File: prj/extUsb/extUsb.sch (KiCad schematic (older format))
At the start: 6 parts, among them J1 USB_B_Micro, J2 Conn_01x05, U1 SN74LVC2T45

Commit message: extUsb Redo after attempt2 experiments and add 3.3V rail.
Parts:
- added C1, C2: 18p, Capacitor_SMD:C_0603_1608Metric_Pad1.08x0.95mm_HandSolder, symbol Device:C
- added C3, C4: 100n, Capacitor_SMD:C_0603_1608Metric_Pad1.08x0.95mm_HandSolder, symbol Device:C
- added C5: 10u, Capacitor_SMD:C_0603_1608Metric_Pad1.08x0.95mm_HandSolder, symbol Device:C
- added FB1: Ferrite_Bead, Inductor_SMD:L_0603_1608Metric_Pad1.05x0.95mm_HandSolder, symbol Device:Ferrite_Bead
- added Q1: Q_NMOS_GSD, Package_TO_SOT_SMD:SOT-23_Handsoldering, symbol Device:Q_NMOS_GSD
- added R4: 10k, Resistor_SMD:R_0603_1608Metric_Pad0.98x0.95mm_HandSolder, symbol Device:R
- added U2: MIC5504-3.3YM5, Package_TO_SOT_SMD:SOT-23-5, symbol Regulator_Linear:MIC5504-3.3YM5
- R1: renamed from R2; value 68 -> 33
- R2: renamed from R3; value 68 -> 33
- renumbered R1 to R3
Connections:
- net labels added: +3.3V, +5V
- net labels removed: Vusb
- wire segments 29 -> 35
- no-connect marks 2 -> 1
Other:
- moved on the sheet: J1, J2, R1, R2, R3, U1

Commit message: extUsb Annotate schematic
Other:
- note added: "1.0.0"
- note added: "2020-10-31"
- note added: "FB1 blocks noise from propagating to USB host power supply,\nand works in conjunction with C5 to stabilize +5V.\nC3, C4, and C5 bypass capacitors stabilize power supplies.\nU2 provides 3.3V, as required by USB."
- note added: "J2 separated via labels to simplify pin re-assignment."
- note added: "Levelshifter for low or unknown voltage (1.65V..5.5V) logic implementing USB Full Speed protocol.\nFor example, FPGA with protocol implemented in logic, or a MCU bit-banging the protocol."
- note added: "R1 and R2 series termination protect D+,D- transmission lines against device-to-host transient voltage spikes.\nOptionally (with C1,C2) include low-pass filtering."
- note added: "R3 pullup to 3.3V indicates USB-FullSpeed to host, enabled by connecting Vext.\nWhen Vext is unconnected, R4 pulldown on Q1 disables the R3 pullup, indicating "no device" to host."
- note added: "extUsb"
- moved on the sheet: C1, C2, C3, C4, C5, FB1, J1, J2, R1, R2, R3, R4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

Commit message: extUsb Layout for hand-solder
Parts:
- U2: footprint Package_TO_SOT_SMD:SOT-23-5 -> Package_TO_SOT_SMD:SOT-23-5_HandSoldering
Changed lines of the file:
@@
 F 0 "U2" H 2900 2267 50  0000 C CNN
 F 1 "MIC5504-3.3YM5" H 2900 2176 50  0000 C CNN
-F 2 "Package_TO_SOT_SMD:SOT-23-5" H 2900 1500 50  0001 C CNN
+F 2 "Package_TO_SOT_SMD:SOT-23-5_HandSoldering" H 2900 1500 50  0001 C CNN
 F 3 "http://ww1.microchip.com/downloads/en/DeviceDoc/MIC550X.pdf" H 2650 2150 50  0001 C CNN
 	1    2900 1900

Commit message: extUsb Analog switch for 1k5 pullup
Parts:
- removed Q1: Q_NMOS_GSD, Package_TO_SOT_SMD:SOT-23_Handsoldering, symbol Device:Q_NMOS_GSD
- added U3: TS5A3166DBVR, Package_TO_SOT_SMD:SOT-23-5, symbol Analog_Switch:TS5A3166DBVR
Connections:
- wire segments 35 -> 41
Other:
- note added: "R3 pullup to 3.3V indicates USB-FullSpeed to host, enabled by connecting Vext.\nWhen Vext is unconnected, R4 pulldown on U3 disables the R3 pullup, indicating "no device" to host."
- note removed: "R3 pullup to 3.3V indicates USB-FullSpeed to host, enabled by connecting Vext.\nWhen Vext is unconnected, R4 pulldown on Q1 disables the R3 pullup, indicating "no device" to host."
- moved on the sheet: R4
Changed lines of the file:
@@
 L power:+3.3V #PWR01
 U 1 1 5FA00B0B
-P 1700 5100
-F 0 "#PWR01" H 1700 4950 50  0001 C CNN
-F 1 "+3.3V" H 1715 5273 50  0000 C CNN
-F 2 "" H 1700 5100 50  0001 C CNN
-F 3 "" H 1700 5100 50  0001 C CNN
-	1    1700 5100
+P 1050 5000
+F 0 "#PWR01" H 1050 4850 50  0001 C CNN
+F 1 "+3.3V" H 1065 5173 50  0000 C CNN
+F 2 "" H 1050 5000 50  0001 C CNN
+F 3 "" H 1050 5000 50  0001 C CNN
+	1    1050 5000
 	1    0    0    -1
 $EndComp
@@
 	1950 1800 2200 1800
 $Comp
-L Device:Q_NMOS_GSD Q1
-U 1 1 5FA2F162
-P 1600 5300
-F 0 "Q1" H 1804 5346 50  0000 L CNN
-F 1 "Q_NMOS_GSD" H 1804 5255 50  0000 L CNN
-F 2 "Package_TO_SOT_SMD:SOT-23_Handsoldering" H 1800 5400 50  0001 C CNN
-F 3 "https://www.vishay.com/docs/63302/si2342ds.pdf" H 1600 5300 50  0001 C CNN
-	1    1600 5300
-	1    0    0    -1
-$EndComp
-$Comp
 L Device:R R4
 U 1 1 5FA4650C
-P 1350 5450
-F 0 "R4" H 1400 5400 50  0000 L CNN
-F 1 "10k" V 1350 5350 50  0000 L CNN
-F 2 "Resistor_SMD:R_0603_1608Metric_Pad0.98x0.95mm_HandSolder" V 1280 5450 50  0001 C CNN
-F 3 "~" H 1350 5450 50  0001 C CNN
-	1    1350 5450
+P 1000 5550
+F 0 "R4" H 1050 5500 50  0000 L CNN
+F 1 "10k" V 1000 5450 50  0000 L CNN
+F 2 "Resistor_SMD:R_0603_1608Metric_Pad0.98x0.95mm_HandSolder" V 930 5550 50  0001 C CNN
+F 3 "~" H 1000 5550 50  0001 C CNN
+	1    1000 5550
 	1    0    0    -1
 $EndComp
 Wire Wire Line
 	1300 6100 1700 6100
-Text GLabel 1300 5300 0    50   Input ~ 0
+Text GLabel 950  5400 0    50   Input ~ 0
 Vext
 $Comp
 L power:GND #PWR0103
 U 1 1 5FA4C220
-P 1350 5600
-F 0 "#PWR0103" H 1350 5350 50  0001 C CNN
-F 1 "GND" H 1355 5427 50  0000 C CNN
-F 2 "" H 1350 5600 50  0001 C CNN
-F 3 "" H 1350 5600 50  0001 C CNN
-	1    1350 5600
+P 1000 5700
+F 0 "#PWR0103" H 1000 5450 50  0001 C CNN
+F 1 "GND" H 1005 5527 50  0000 C CNN
+F 2 "" H 1000 5700 50  0001 C CNN
+F 3 "" H 1000 5700 50  0001 C CNN
+	1    1000 5700
 	1    0    0    -1
 $EndComp
@@
 	1700 5800 1700 6100
 Wire Wire Line
-	1300 5300 1350 5300
-Connection ~ 1350 5300
+	950  5400 1000 5400
+Connection ~ 1000 5400
 Wire Wire Line
-	1350 5300 1400 5300
+	1000 5400 1050 5400
 Text Notes 1000 4800 0    50   ~ 0
-R3 pullup to 3.3V indicates USB-FullSpeed to host, enabled by connecting Vext.\nWhen Vext is unconnected, R4 pulldown on Q1 disables the R3 pullup, indicating "no device" to host.
+R3 pullup to 3.3V indicates USB-FullSpeed to host, enabled by connecting Vext.\nWhen Vext is unconnected, R4 pulldown on U3 disables the R3 pullup, indicating "no device" to host.
 Text Notes 1000 7450 0    50   ~ 0
 R1 and R2 series termination protect D+,D- transmission lines against device-to-host transient voltage spikes.\nOptionally (with C1,C2) include low-pass filtering.
@@
 Text Notes 10600 7650 0    50   ~ 0
 1.0.0
+$Comp
+L Analog_Switch:TS5A3166DBVR U3
+U 1 1 5FA73056
+P 1350 5300
+F 0 "U3" H 1250 5450 50  0000 L CNN
+F 1 "TS5A3166DBVR" H 1150 5200 50  0000 L CNN
+F 2 "Package_TO_SOT_SMD:SOT-23-5" H 1300 5150 50  0001 C CNN
+F 3 " http://www.ti.com/lit/ds/symlink/ts5a3166.pdf" H 1350 5400 50  0001 C CNN
+	1    1350 5300
+	1    0    0    -1
+$EndComp
+Wire Wire Line
+	1450 5600 1450 5700
+Wire Wire Line
+	1450 5700 1000 5700
+Connection ~ 1000 5700
+Wire Wire Line
+	1050 5300 1050 5000
+Wire Wire Line
+	1050 5000 1450 5000
+Connection ~ 1050 5000
+Wire Wire Line
+	1650 5300 1700 5300
+Wire Wire Line
+	1700 5300 1700 5500
 $EndSCHEMATC

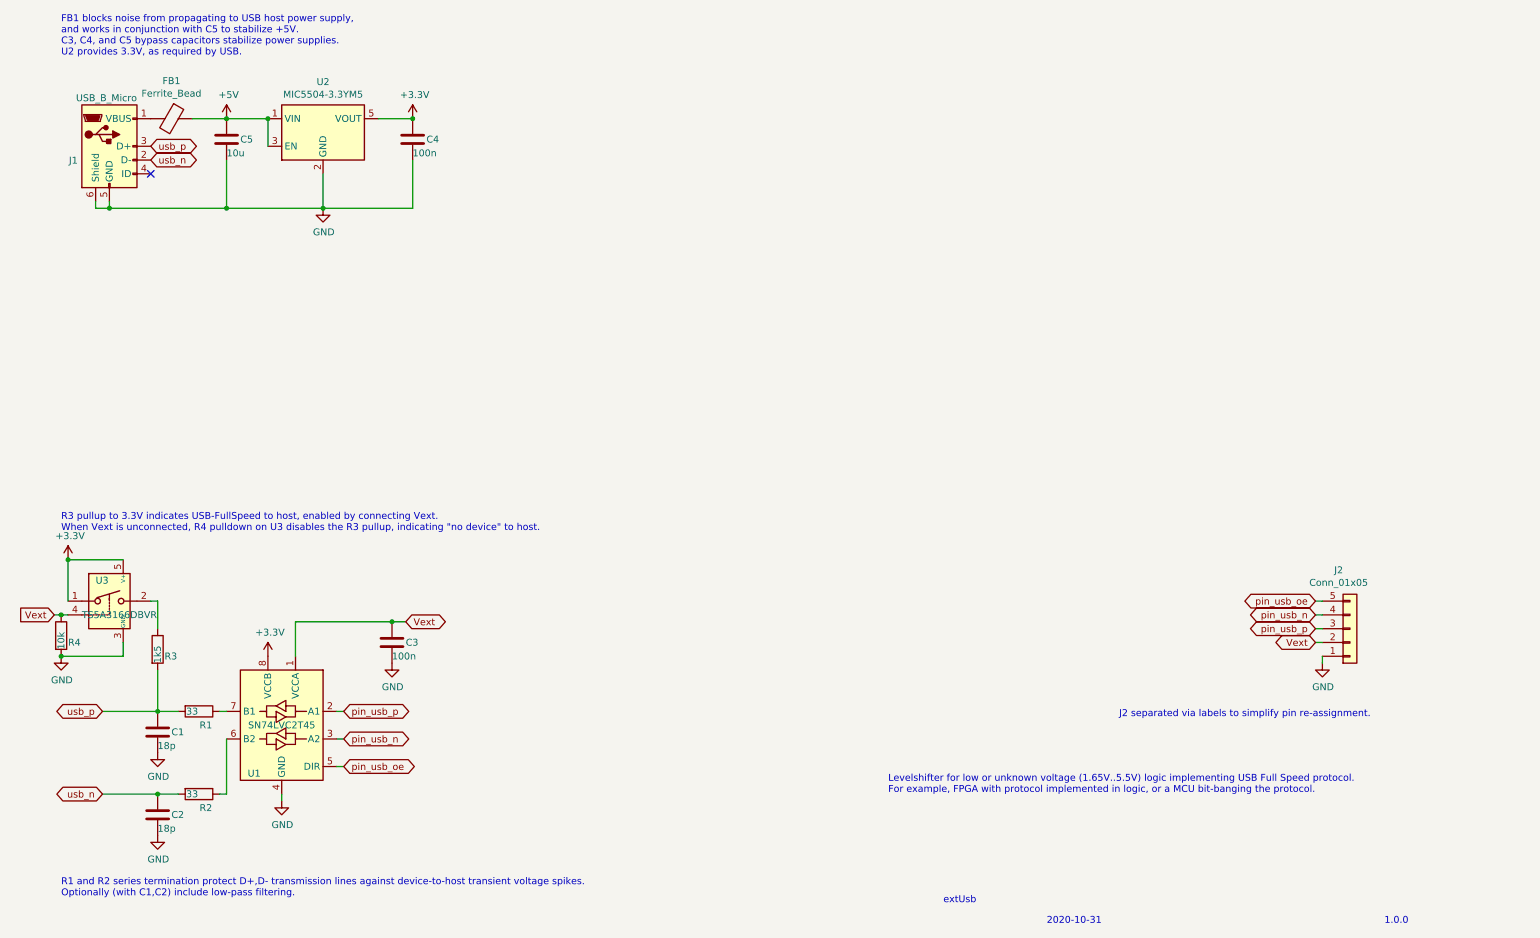
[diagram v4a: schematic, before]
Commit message: extUsb Testpoints and many minor improvements to layout.
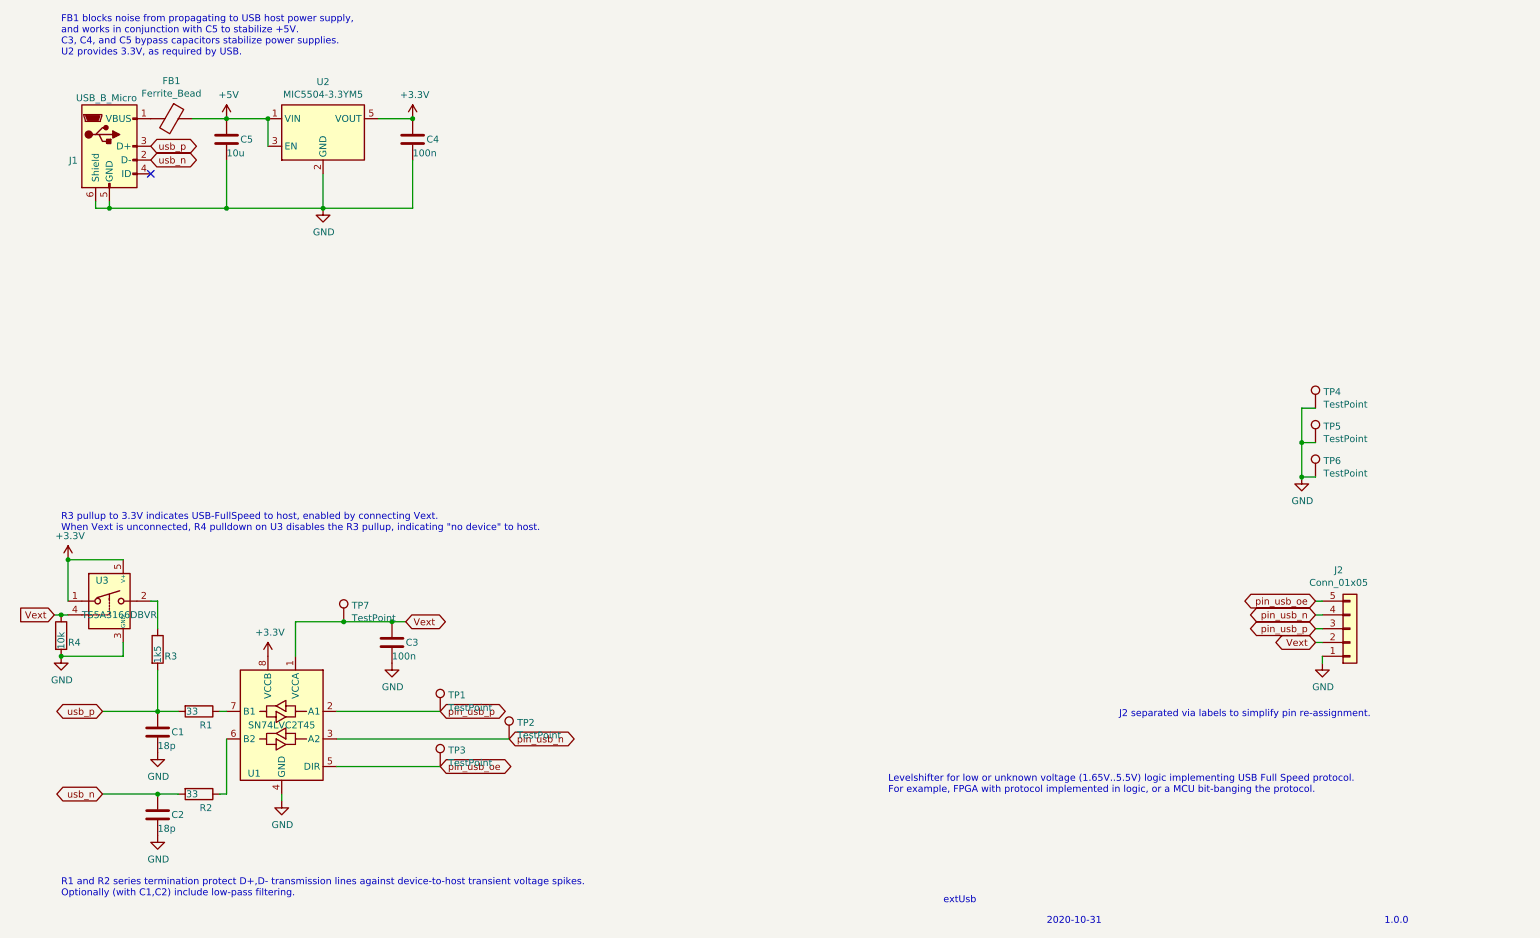
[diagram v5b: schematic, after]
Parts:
- added TP1: TestPoint, symbol Connector:TestPoint
- added TP2, TP3, TP4, TP5, TP6, TP7: TestPoint, TestPoint:TestPoint_Pad_D2.0mm, symbol Connector:TestPoint
- U3: footprint Package_TO_SOT_SMD:SOT-23-5 -> Package_TO_SOT_SMD:SOT-23-5_HandSoldering
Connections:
- net GND: now also TP4.1, TP5.1, TP6.1
- net Vext: now also TP7.1
- net pin_usb_n: now also TP2.1
- net pin_usb_oe: now also TP3.1
- net pin_usb_p: now also TP1.1
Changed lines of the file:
@@
 Text GLabel 3500 5450 2    50   BiDi ~ 0
 Vext
-Text GLabel 3050 6100 2    50   BiDi ~ 0
+Text GLabel 3750 6100 2    50   BiDi ~ 0
 pin_usb_p
-Text GLabel 3050 6300 2    50   BiDi ~ 0
+Text GLabel 4250 6300 2    50   BiDi ~ 0
 pin_usb_n
-Text GLabel 3050 6500 2    50   BiDi ~ 0
+Text GLabel 3750 6500 2    50   BiDi ~ 0
 pin_usb_oe
 Text GLabel 10100 5500 0    50   BiDi ~ 0
@@
 Text GLabel 10100 5300 0    50   BiDi ~ 0
 pin_usb_oe
-Wire Wire Line
-	3000 6100 3050 6100
-Wire Wire Line
-	3000 6300 3050 6300
-Wire Wire Line
-	3000 6500 3050 6500
 Wire Wire Line
 	10150 5300 10100 5300
@@
 	1    0    0    -1
 $EndComp
-Wire Wire Line
-	3300 1800 3550 1800
 Connection ~ 3550 1800
 $Comp
@@
 	1    0    0    -1
 $EndComp
-Wire Wire Line
-	2200 1800 2500 1800
 Connection ~ 2500 1800
 Wire Wire Line
@@
 $EndComp
 Wire Wire Line
-	3400 5450 2700 5450
-Wire Wire Line
 	2700 5450 2700 5700
 $Comp
@@
 Wire Wire Line
 	1700 6700 1850 6700
-Wire Wire Line
-	1300 6700 1700 6700
 $Comp
 L Logic_LevelTranslator:SN74LVC2T45DCUR U1
@@
 	1    0    0    -1
 $EndComp
-Wire Wire Line
-	1300 6100 1700 6100
 Text GLabel 950  5400 0    50   Input ~ 0
 Vext
@@
 Text Notes 10600 7650 0    50   ~ 0
 1.0.0
+Wire Wire Line
+	1450 5600 1450 5700
+Wire Wire Line
+	1450 5700 1000 5700
+Connection ~ 1000 5700
+Wire Wire Line
+	1050 5300 1050 5000
+Wire Wire Line
+	1050 5000 1450 5000
+Connection ~ 1050 5000
+Wire Wire Line
+	1650 5300 1700 5300
+Wire Wire Line
+	1700 5300 1700 5500
 $Comp
 L Analog_Switch:TS5A3166DBVR U3
@@
 F 0 "U3" H 1250 5450 50  0000 L CNN
 F 1 "TS5A3166DBVR" H 1150 5200 50  0000 L CNN
-F 2 "Package_TO_SOT_SMD:SOT-23-5" H 1300 5150 50  0001 C CNN
+F 2 "Package_TO_SOT_SMD:SOT-23-5_HandSoldering" H 1300 5150 50  0001 C CNN
 F 3 " http://www.ti.com/lit/ds/symlink/ts5a3166.pdf" H 1350 5400 50  0001 C CNN
 	1    1350 5300
@@
 $EndComp
 Wire Wire Line
-	1450 5600 1450 5700
-Wire Wire Line
-	1450 5700 1000 5700
-Connection ~ 1000 5700
-Wire Wire Line
-	1050 5300 1050 5000
-Wire Wire Line
-	1050 5000 1450 5000
-Connection ~ 1050 5000
-Wire Wire Line
-	1650 5300 1700 5300
-Wire Wire Line
-	1700 5300 1700 5500
+	3400 5450 3050 5450
+Wire Wire Line
+	3300 1800 3550 1800
+Wire Wire Line
+	2200 1800 2500 1800
+$Comp
+L Connector:TestPoint TP2
+U 1 1 5FA881AA
+P 4250 6300
+F 0 "TP2" H 4308 6418 50  0000 L CNN
+F 1 "TestPoint" H 4308 6327 50  0000 L CNN
+F 2 "TestPoint:TestPoint_Pad_D2.0mm" H 4450 6300 50  0001 C CNN
+F 3 "~" H 4450 6300 50  0001 C CNN
+	1    4250 6300
+	1    0    0    -1
+$EndComp
+$Comp
+L Connector:TestPoint TP1
+U 1 1 5FA87D46
+P 3750 6100
+F 0 "TP1" H 3808 6218 50  0000 L CNN
+F 1 "TestPoint" H 3808 6127 50  0000 L CNN
+F 2 "" H 3950 6100 50  0001 C CNN
+F 3 "~" H 3950 6100 50  0001 C CNN
+	1    3750 6100
+	1    0    0    -1
+$EndComp
+Wire Wire Line
+	3000 6100 3750 6100
+Wire Wire Line
+	1300 6700 1700 6700
+Wire Wire Line
+	1300 6100 1700 6100
+Wire Wire Line
+	3000 6300 4250 6300
+$Comp
+L Connector:TestPoint TP4
+U 1 1 5FAA3783
+P 10100 3900
+F 0 "TP4" H 10158 4018 50  0000 L CNN
+F 1 "TestPoint" H 10158 3927 50  0000 L CNN
+F 2 "TestPoint:TestPoint_Pad_D2.0mm" H 10300 3900 50  0001 C CNN
+F 3 "~" H 10300 3900 50  0001 C CNN
+	1    10100 3900
+	1    0    0    -1
+$EndComp
+$Comp
+L Connector:TestPoint TP5
+U 1 1 5FAA3DCC
+P 10100 4150
+F 0 "TP5" H 10158 4268 50  0000 L CNN
+F 1 "TestPoint" H 10158 4177 50  0000 L CNN
+F 2 "TestPoint:TestPoint_Pad_D2.0mm" H 10300 4150 50  0001 C CNN
+F 3 "~" H 10300 4150 50  0001 C CNN
+	1    10100 4150
+	1    0    0    -1
+$EndComp
+$Comp
+L Connector:TestPoint TP6
+U 1 1 5FAA4E02
+P 10100 4400
+F 0 "TP6" H 10158 4518 50  0000 L CNN
+F 1 "TestPoint" H 10158 4427 50  0000 L CNN
+F 2 "TestPoint:TestPoint_Pad_D2.0mm" H 10300 4400 50  0001 C CNN
+F 3 "~" H 10300 4400 50  0001 C CNN
+	1    10100 4400
+	1    0    0    -1
+$EndComp
+$Comp
+L Connector:TestPoint TP3
+U 1 1 5FAA52CF
+P 3750 6500
+F 0 "TP3" H 3808 6618 50  0000 L CNN
+F 1 "TestPoint" H 3808 6527 50  0000 L CNN
+F 2 "TestPoint:TestPoint_Pad_D2.0mm" H 3950 6500 50  0001 C CNN
+F 3 "~" H 3950 6500 50  0001 C CNN
+	1    3750 6500
+	1    0    0    -1
+$EndComp
+Wire Wire Line
+	3000 6500 3750 6500
+$Comp
+L power:GND #PWR0104
+U 1 1 5FAA8E6F
+P 10000 4400
+F 0 "#PWR0104" H 10000 4150 50  0001 C CNN
+F 1 "GND" H 10005 4227 50  0000 C CNN
+F 2 "" H 10000 4400 50  0001 C CNN
+F 3 "" H 10000 4400 50  0001 C CNN
+	1    10000 4400
+	1    0    0    -1
+$EndComp
+Wire Wire Line
+	10000 4400 10100 4400
+Wire Wire Line
+	10000 4400 10000 4150
+Wire Wire Line
+	10000 3900 10100 3900
+Connection ~ 10000 4400
+Wire Wire Line
+	10100 4150 10000 4150
+Connection ~ 10000 4150
+Wire Wire Line
+	10000 4150 10000 3900
+$Comp
+L Connector:TestPoint TP7
+U 1 1 5FAB2342
+P 3050 5450
+F 0 "TP7" H 3108 5568 50  0000 L CNN
+F 1 "TestPoint" H 3108 5477 50  0000 L CNN
+F 2 "TestPoint:TestPoint_Pad_D2.0mm" H 3250 5450 50  0001 C CNN
+F 3 "~" H 3250 5450 50  0001 C CNN
+	1    3050 5450
+	1    0    0    -1
+$EndComp
+Connection ~ 3050 5450
+Wire Wire Line
+	3050 5450 2700 5450
 $EndSCHEMATC
